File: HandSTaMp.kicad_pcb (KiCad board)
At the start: 2 copper layers, 40.6 x 16.5 mm, 24 parts, among them J1 USB_C_Receptacle_USB2.0_16P, J2 SWD, J3 Pins, SW0 BOOT, SW1 Row 0, Col+0, SW2 Row 0, Col+1, U1 STM32C071GBUx, U2 PRTR5V0U2X, U3 XC6206P332MR-G

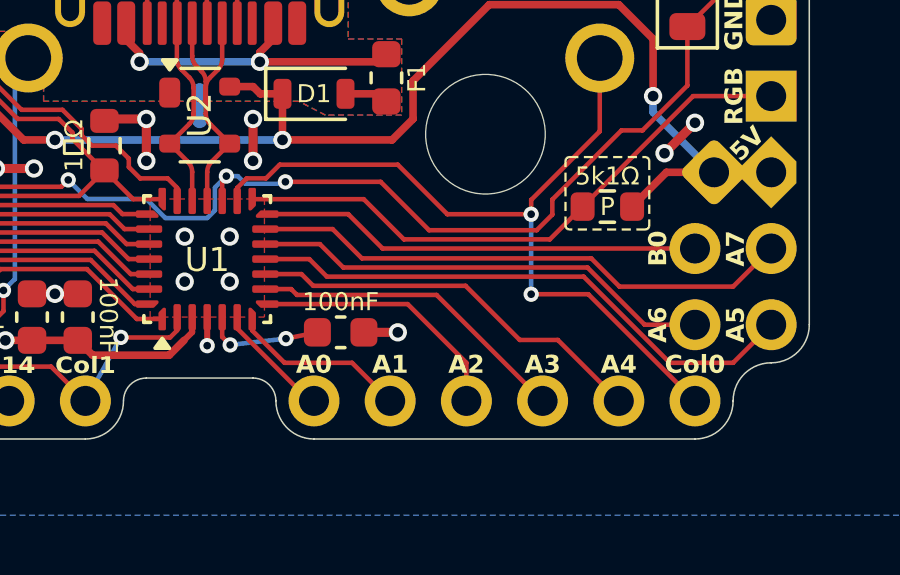
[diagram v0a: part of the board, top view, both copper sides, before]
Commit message: Add access to PF2-NRST
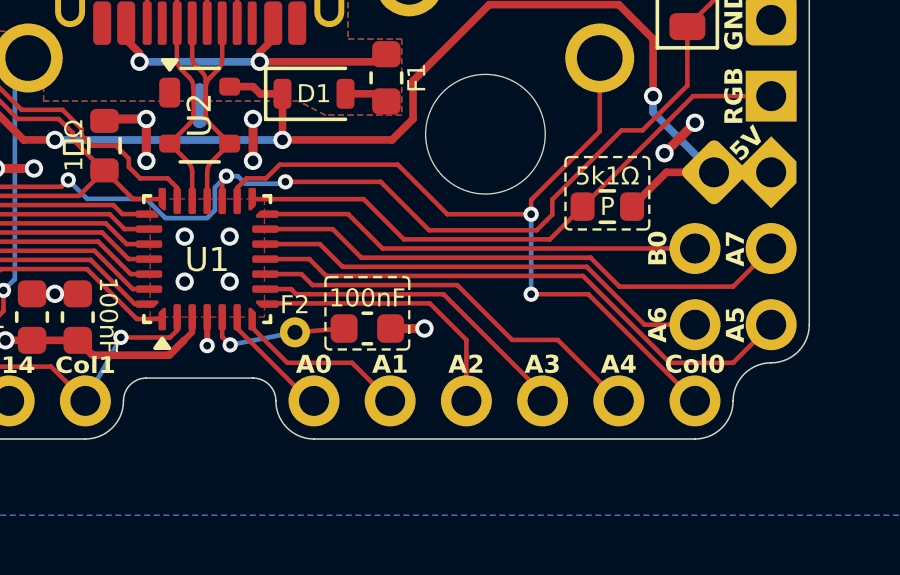
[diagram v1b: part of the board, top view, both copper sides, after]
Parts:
- added J4: F2, TestPoint:TestPoint_THTPad_D1.0mm_Drill0.5mm, F.Cu at (104.8, 57.4)
- moved C5 0.90 mm to (107.2, 57.3)
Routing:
- net NRST: track 3.97 -> 4.88 mm, vias 2 -> 1
